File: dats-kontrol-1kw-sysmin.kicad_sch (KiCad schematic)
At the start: 26 parts, among them J1 SWD, J3 USB_B, J7 Conn_01x12, SW1 SW?, U1 AMS1117CD-3.3, U2 STM32F4X1CXU6, Y1 25MHZ 9PF, Y2 32.768KHz

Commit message: new layout
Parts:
- removed C1: 10uF, Capacitor_SMD:C_0805_2012Metric, symbol Device:C
- added C1, C14: 10 uF, Capacitor_SMD:CP_Elec_5x5.3, symbol Device:C_Polarized
- added U3: L7805, Package_TO_SOT_SMD:TO-252-2, symbol Regulator_Linear:L7805
- added U4: XT30PW-F, XT30:XT30PW-F, symbol XT30PW-F:XT30PW-F
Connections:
- net +5V: now also C1.1, U3.3 (OUT)
- net GND: now also C2.2, C3.2, C4.2, C5.2, C7.2, C1.2, C14.2, U3.2 (GND), U4.P1 (-)
- net at J3.2 (D-), U2.32 (PA11): now also J3.3 (D+), U2.33 (PA12)
- removed net Earth: C2.2, C3.2, C4.2, C5.2, C7.2, U2.35 (VSS), U2.47 (VSS), U2.49 (VSS), U2.8 (VSSA)
- new net: U2.35 (VSS), U2.47 (VSS), U2.49 (VSS)
- new net +12V: C14.1, U3.1 (IN), U4.P2 (+)
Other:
- moved on the sheet: C11, C12, C13, C2, C3, C4, C5, C6, C7, C8, C9, D1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

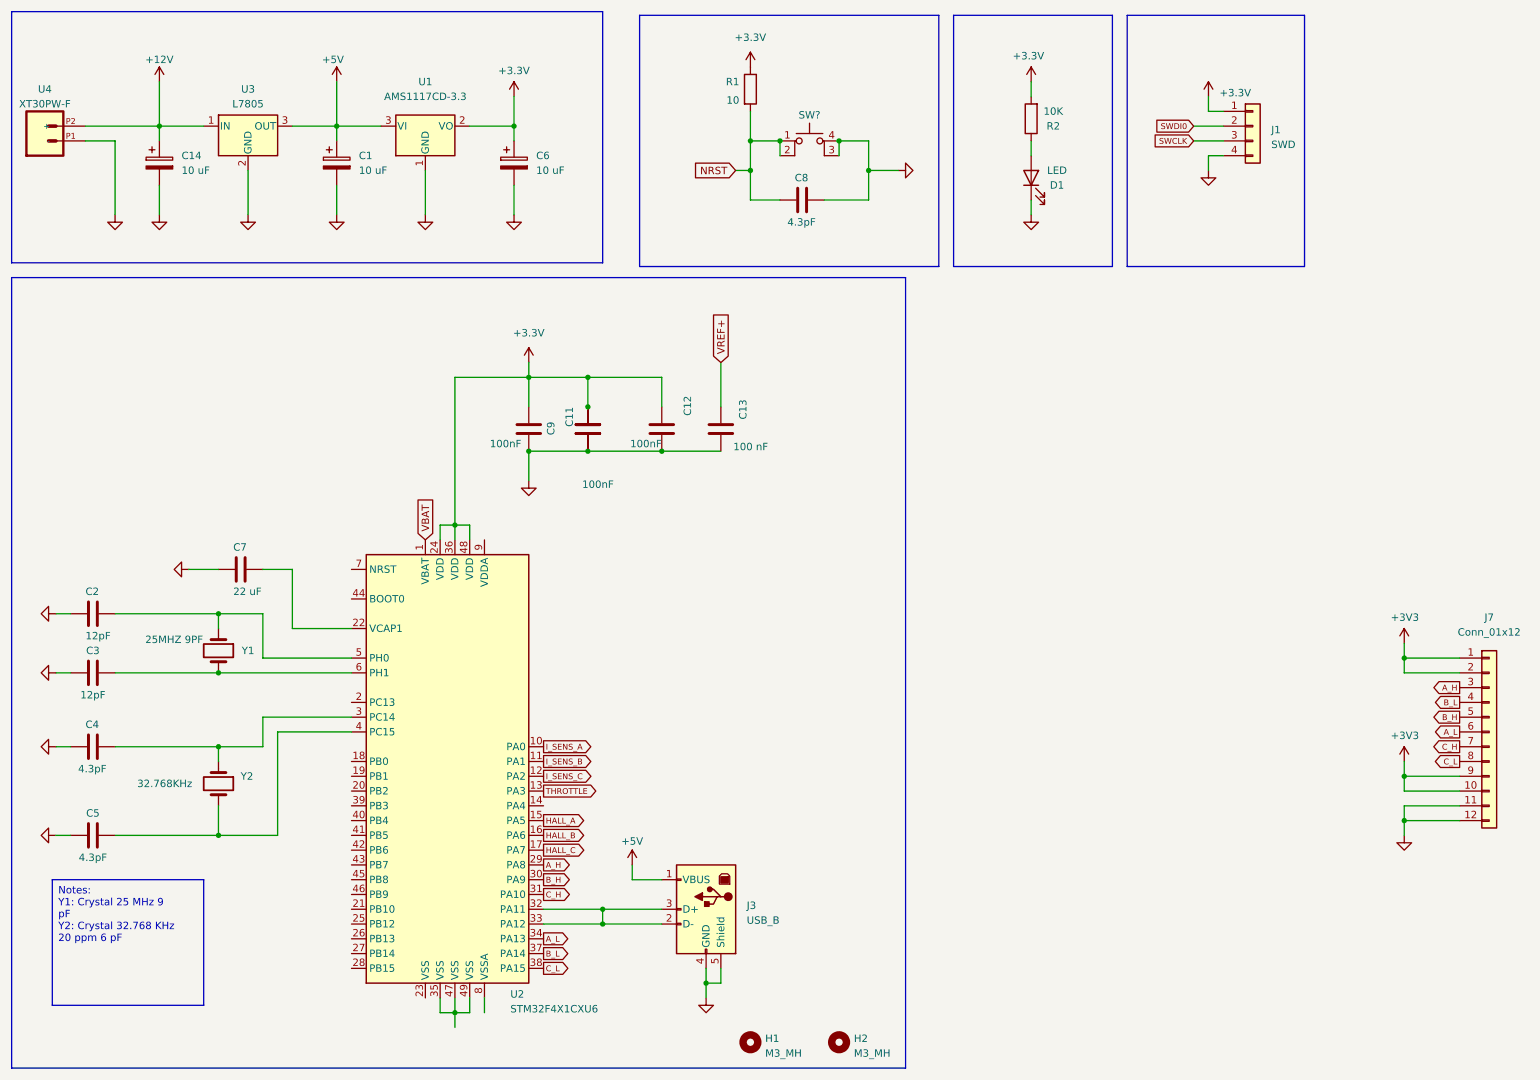
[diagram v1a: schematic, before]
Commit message: adding stm32 symbol+footprint
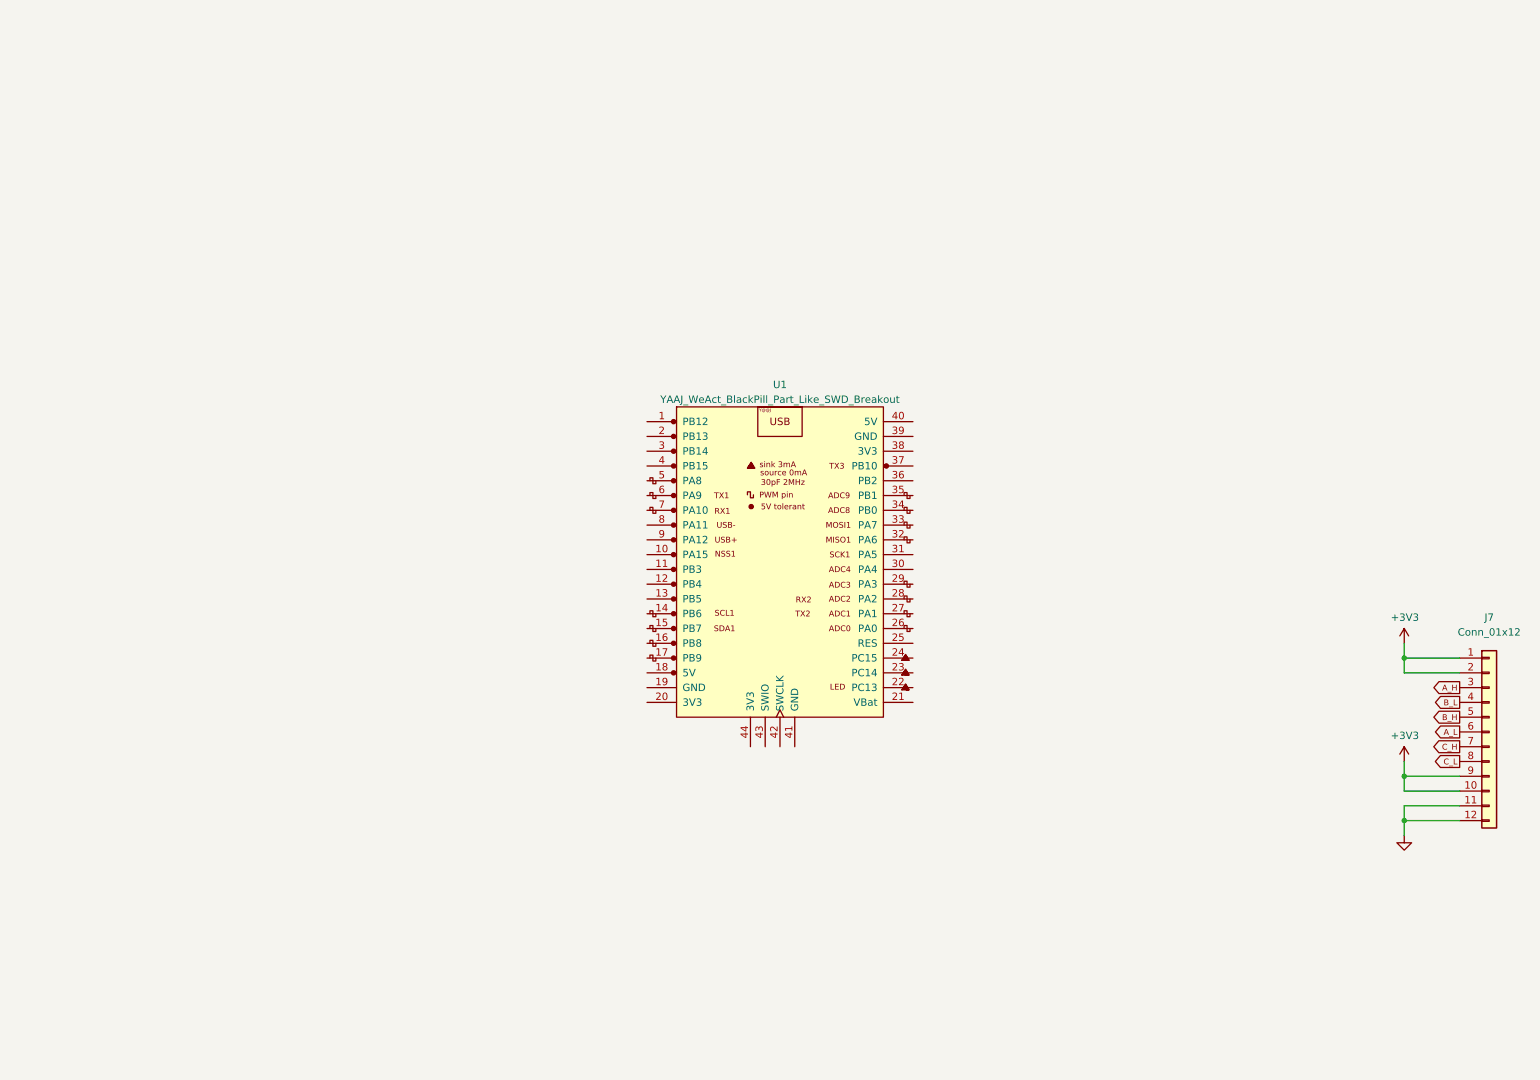
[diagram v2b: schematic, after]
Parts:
- removed C1, C14, C6: 10 uF, Capacitor_SMD:CP_Elec_5x5.3, symbol Device:C_Polarized
- removed C10, C11, C12, C9: 100nF, Capacitor_SMD:C_0805_2012Metric, symbol Device:C
- removed C13: 100 nF, Capacitor_SMD:C_0805_2012Metric, symbol Device:C
- removed C2, C3: 12pF, Capacitor_SMD:C_0805_2012Metric, symbol Device:C
- removed C4, C5, C8: 4.3pF, Capacitor_SMD:C_0805_2012Metric, symbol Device:C
- removed C7: 22 uF, Capacitor_SMD:C_0805_2012Metric, symbol Device:C
- removed D1: LED, LED_SMD:LED_0805_2012Metric, symbol Device:LED
- removed H1, H2: M3_MH, MountingHole:MountingHole_3.2mm_M3, symbol Mechanical:MountingHole
- removed J1: SWD, Connector_PinHeader_2.54mm:PinHeader_1x04_P2.54mm_Vertical, symbol Connector_Generic:Conn_01x04
- removed J3: USB_B, Connector_USB:USB_B_TE_5787834_Vertical, symbol Connector:USB_B
- removed R1: 10, Resistor_SMD:R_0805_2012Metric, symbol Device:R
- removed R2: 10K, Resistor_SMD:R_0805_2012Metric, symbol Device:R
- removed SW1: SW?, Button_Switch_SMD:SW_Push_1P1T_NO_CK_KMR2, symbol Switch:SW_MEC_5E
- removed U1: AMS1117CD-3.3, Package_TO_SOT_SMD:SOT-223-3_TabPin2, symbol Regulator_Linear:AMS1117CD-3.3
- removed U2: STM32F4X1CXU6, Package_DFN_QFN:QFN-48-1EP_7x7mm_P0.5mm_EP5.6x5.6mm, symbol MCU_ST_STM32F4:STM32F411CCUx
- removed U3: L7805, Package_TO_SOT_SMD:TO-252-2, symbol Regulator_Linear:L7805
- removed U4: XT30PW-F, XT30:XT30PW-F, symbol XT30PW-F:XT30PW-F
- removed Y1: 25MHZ 9PF, Crystal:Crystal_SMD_3225-4Pin_3.2x2.5mm_HandSoldering, symbol Device:Crystal
- removed Y2: 32.768KHz, Crystal:Crystal_SMD_SeikoEpson_MC146-4Pin_6.7x1.5mm_HandSoldering, symbol Device:Crystal
- added U1: YAAJ_WeAct_BlackPill_Part_Like_SWD_Breakout, blackpill:YAAJ_WeAct_BlackPill_2, symbol YAAJ_WeAct_BlackPill_Part_Like_SWD_Breakout:YAAJ_WeAct_BlackPill_Part_Like_SWD_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

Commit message: Layout STM
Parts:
- added C1: C, Resistor_SMD:R_0805_2012Metric, symbol Device:C
- added J1, J2, J3: Conn_01x03, Connector_PinHeader_2.54mm:PinHeader_1x03_P2.54mm_Vertical, symbol Connector_Generic:Conn_01x03
- added J5: Conn_01x05, Connector_JST:JST_XH_B5B-XH-A_1x05_P2.50mm_Vertical, symbol Connector_Generic:Conn_01x05
- added J6: Conn_01x03, Connector_JST:JST_XH_B3B-XH-A_1x03_P2.50mm_Vertical, symbol Connector_Generic:Conn_01x03
- added J7: Conn_01x02, Connector_JST:JST_XH_B2B-XH-A_1x02_P2.50mm_Vertical, symbol Connector_Generic:Conn_01x02
- added R1, R2, R3: 10K, Resistor_SMD:R_0805_2012Metric, symbol Device:R_Small
- added R4: 1K, Resistor_SMD:R_0805_2012Metric, symbol Device:R
- added R5: 120, Resistor_SMD:R_0805_2012Metric, symbol Device:R
- added U2: MCP2551-I-SN, Package_SO:SOIC-8_3.9x4.9mm_P1.27mm, symbol Interface_CAN_LIN:MCP2551-I-SN
- J7: footprint Connector_PinHeader_2.54mm:PinHeader_1x12_P2.54mm_Vertical -> Connector_PinHeader_2.54mm:PinHeader_2x06_P2.54mm_Vertical
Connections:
- net +3V3: now also U1.20 (3V3), U1.38 (3V3), J1.1 (Pin_1), J2.1 (Pin_1), J3.1 (Pin_1), J5.4 (Pin_4), J6.1 (Pin_1), R1.1, R2.1, R3.1
- net A_H: now also U1.5 (PA8)
- net A_L: now also J7.4 (Pin_4), U1.2 (PB13); no longer J7.6 (Pin_6)
- net B_H: now also U1.6 (PA9)
- net B_L: now also J7.6 (Pin_6), U1.3 (PB14); no longer J7.4 (Pin_4)
- net C_H: now also U1.7 (PA10)
- net C_L: now also U1.4 (PB15)
- net GND: now also U1.19 (GND), U1.39 (GND), C1.2, J1.3 (Pin_3), J2.3 (Pin_3), J3.3 (Pin_3), J5.5 (Pin_5), J6.3 (Pin_3), R4.1, U2.2 (VSS)
- net CAN_TX: now reaches U1.10 (PA15)
- net CAN_TX: now also U2.1 (TXD)
- net CAN_RX: now reaches U1.11 (PB3)
- net CAN_RX: now also U2.4 (RXD)
- net HALL_A: now reaches U1.12 (PB4)
- net HALL_A: now also J5.1 (Pin_1), R1.2
- net HALL_B: now reaches U1.13 (PB5)
- net HALL_B: now also J5.2 (Pin_2), R2.2
- net HALL_C: now reaches U1.14 (PB6)
- net HALL_C: now also J5.3 (Pin_3), R3.2
- net CURRENT_SENS_C: now reaches U1.30 (PA4)
- net CURRENT_SENS_C: now also J1.2 (Pin_2)
- net THROTTLE: now reaches U1.31 (PA5)
- net THROTTLE: now also J6.2 (Pin_2)
- net CURRENT_SENS_A: now reaches U1.34 (PB0)
- net CURRENT_SENS_A: now also J3.2 (Pin_2)
- net CURRENT_SENS_B: now reaches U1.35 (PB1)
- net CURRENT_SENS_B: now also J2.2 (Pin_2)
- net +5V: now reaches U1.40 (5V)
- net +5V: now also C1.1, U2.3 (VDD)
- new net: J7.2 (Pin_2), R5.2, U2.6 (CANL)
- new net: J7.1 (Pin_1), R5.1, U2.7 (CANH)
- new net: R4.2, U2.8 (Rs)
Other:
- moved on the sheet: J7
